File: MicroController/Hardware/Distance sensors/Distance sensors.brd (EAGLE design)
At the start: 87 x 55 mm, 39 parts, among them U1 LM2937IMP-5.0, U2 TXB0108PWR, U3 TLV1117-33CDCY, U4 TXB0108PWR, X1 0446200002, X2 0446200002, X3 0446200002

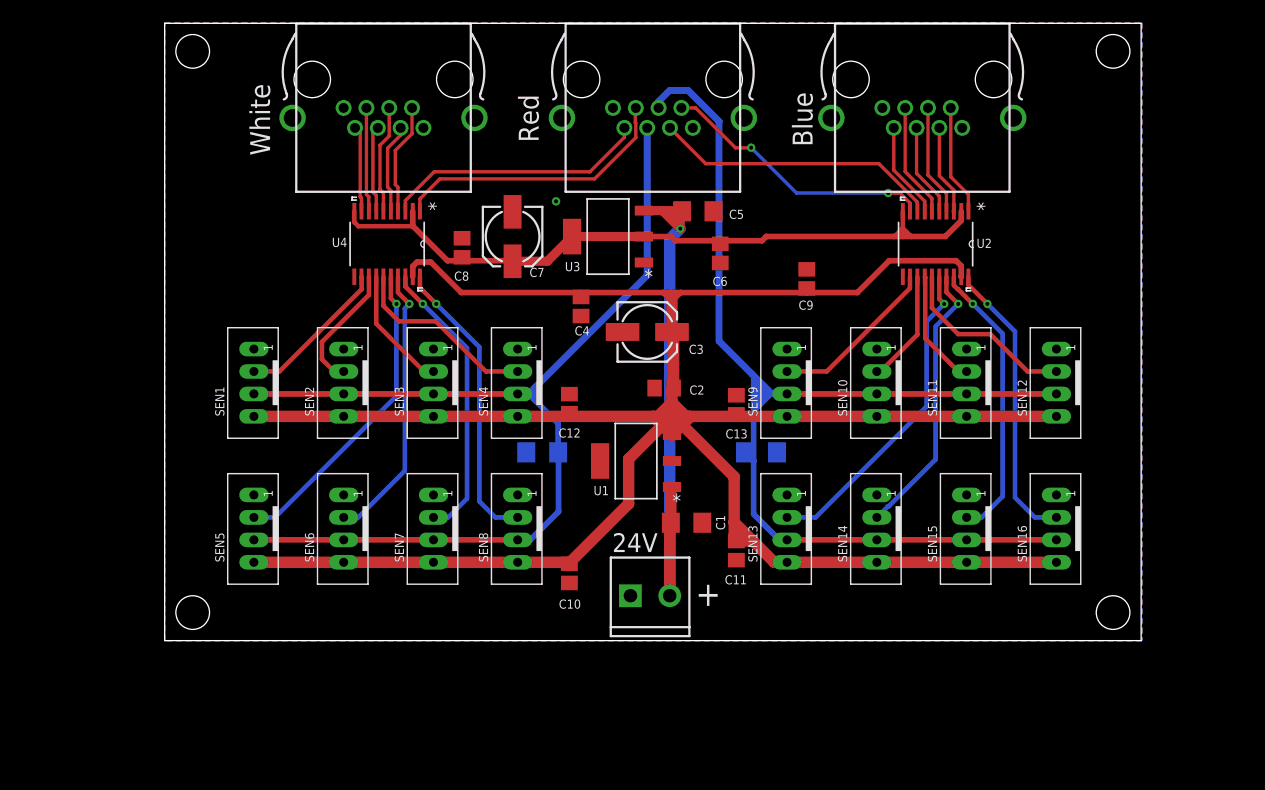
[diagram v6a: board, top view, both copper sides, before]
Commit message: The distance sensor PCB is close to finished.
There needs to be a final check before ordering the PCB. The PCB is not very complicated compared to the previous version, making it easier to check.
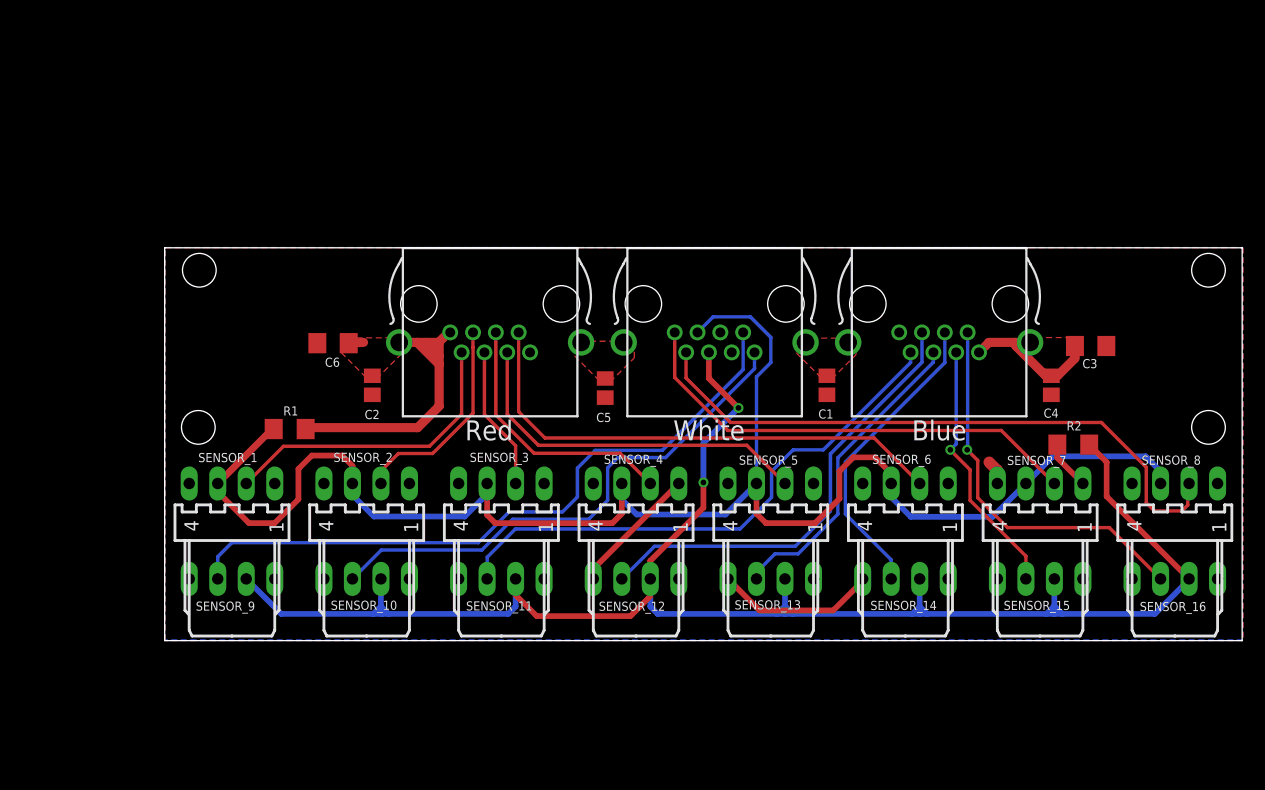
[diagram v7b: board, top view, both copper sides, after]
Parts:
- removed 24V: (no value), SparkFun-Connectors:SCREWTERMINAL-3.5MM-2
- removed C10, C11, C12, C13, C8, C9: (no value), adafruit:C0805
- removed C7: (no value), adafruit:153CLV-0505
- removed SEN1, SEN10, SEN11, SEN12, SEN13, SEN14, SEN15, SEN16, SEN2, SEN3, SEN4, SEN5, SEN6, SEN7, SEN8, SEN9: JST-PH_4-PIN_HEADER, SRG:JST_B4B-PH_HEADER
- removed U1: LM2937IMP-5.0, NSC_By_element14_Batch_1.1:SOT230P700X180-4N
- removed U2, U4: TXB0108PWR, Texas Instruments_By_element14_Batch_1:SOP65P640X120-20N
- removed U3: TLV1117-33CDCY, Texas Instruments_By_element14_Batch_1:SOT230P700X180-4N
- added SENSOR_1, SENSOR_10, SENSOR_11, SENSOR_12, SENSOR_13, SENSOR_14, SENSOR_15, SENSOR_16, SENSOR_2, SENSOR_3, SENSOR_4, SENSOR_5, SENSOR_6, SENSOR_7, SENSOR_8, SENSOR_9: 22-05-7048-04, con-molex:7395-04
- C1, C5: device adafruit:C1206 -> adafruit:C0805
- C3: device adafruit:153CLV-0505 -> adafruit:C1206
- C6: device adafruit:C0805 -> adafruit:C1206
- moved C4 42.5 mm to (79.0, 22.8), turned to 90 degrees
- moved C3 39.5 mm to (82.5, 26.2), turned to 180 degrees
- moved C6 35.4 mm to (15.0, 26.5), turned to 0 degrees
- moved R2 27.8 mm to (81.0, 17.5), flipped to the top
- moved C2 26.0 mm to (18.5, 22.8), turned to 90 degrees
- moved R1 22.6 mm to (11.1, 18.9), flipped to the top
- moved X1 22.1 mm to (29.0, 30.0)
- moved X2 20.7 mm to (49.0, 30.0)
- moved X3 20.1 mm to (69.0, 30.0)
- moved C5 17.8 mm to (39.2, 22.5), turned to 90 degrees
- moved C1 17.5 mm to (59.0, 22.8), turned to 90 degrees
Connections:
- removed net +24V: 24V.2, C1.1, C5.1, U1.1, U3.3
- removed net +3V3: C6.1, C7.+, C8.1, U2.10, U2.2, U3.2, U3.4, U4.10, U4.2
- removed net ULTRAS1: SEN1.P2, U4.12
- removed net ULTRAS10: SEN10.P2, U2.13
- removed net ULTRAS11: SEN11.P2, U2.14
- removed net ULTRAS12: SEN12.P2, U2.15
- removed net ULTRAS13: SEN13.P2, U2.16
- removed net ULTRAS14: SEN14.P2, U2.17
- removed net ULTRAS15: SEN15.P2, U2.18
- removed net ULTRAS16: SEN16.P2, U2.20
- removed net ULTRAS2: SEN2.P2, U4.13
- removed net ULTRAS3: SEN3.P2, U4.14
- removed net ULTRAS4: SEN4.P2, U4.15
- removed net ULTRAS5: SEN5.P2, U4.16
- removed net ULTRAS6: SEN6.P2, U4.17
- removed net ULTRAS7: SEN7.P2, U4.18
- removed net ULTRAS8: SEN8.P2, U4.20
- removed net ULTRAS9: SEN9.P2, U2.12
- net +5V: now also C1.1, C3.1, C5.1, C6.1, SENSOR_1.4, SENSOR_10.4, SENSOR_11.4, SENSOR_12.4, SENSOR_13.4, SENSOR_14.4, SENSOR_15.4, SENSOR_16.4, SENSOR_2.4, SENSOR_3.4, SENSOR_4.4, SENSOR_5.4, SENSOR_6.4, SENSOR_7.4, SENSOR_8.4, SENSOR_9.4, X2.5, X2.6; no longer C10.1, C11.1, C12.1, C13.1, C3.+, C9.1, SEN1.P4, SEN10.P4, SEN11.P4, SEN12.P4, SEN13.P4, SEN14.P4, SEN15.P4, SEN16.P4, SEN2.P4, SEN3.P4, SEN4.P4, SEN5.P4, SEN6.P4, SEN7.P4, SEN8.P4, SEN9.P4, U1.3, U2.19, U4.19
- net GND: now also C3.2, SENSOR_1.1, SENSOR_10.1, SENSOR_11.1, SENSOR_12.1, SENSOR_13.1, SENSOR_14.1, SENSOR_15.1, SENSOR_16.1, SENSOR_2.1, SENSOR_3.1, SENSOR_4.1, SENSOR_5.1, SENSOR_6.1, SENSOR_7.1, SENSOR_8.1, SENSOR_9.1; no longer 24V.1, C10.2, C11.2, C12.2, C13.2, C3.-, C7.-, C8.2, C9.2, SEN1.P1, SEN10.P1, SEN11.P1, SEN12.P1, SEN13.P1, SEN14.P1, SEN15.P1, SEN16.P1, SEN2.P1, SEN3.P1, SEN4.P1, SEN5.P1, SEN6.P1, SEN7.P1, SEN8.P1, SEN9.P1, U1.2, U1.4, U2.11, U3.1, U4.11, X2.1, X2.8
- net TRIGGER_1: now also SENSOR_1.3, SENSOR_2.3, SENSOR_3.3, SENSOR_4.3, SENSOR_5.3, SENSOR_6.3, SENSOR_7.3, SENSOR_8.3, X2.3; no longer SEN1.P3, SEN2.P3, SEN3.P3, SEN4.P3, SEN5.P3, SEN6.P3, SEN7.P3, SEN8.P3, X2.4
- net TRIGGER_2: now also SENSOR_10.3, SENSOR_11.3, SENSOR_12.3, SENSOR_13.3, SENSOR_14.3, SENSOR_15.3, SENSOR_16.3, SENSOR_9.3, X2.4; no longer SEN10.P3, SEN11.P3, SEN12.P3, SEN13.P3, SEN14.P3, SEN15.P3, SEN16.P3, SEN9.P3, X2.5
- net ULTRA1: now also SENSOR_1.2; no longer U4.9
- net ULTRA10: now also SENSOR_10.2, X2.8; no longer U2.8, X2.6
- net ULTRA11: now also SENSOR_11.2; no longer U2.7
- net ULTRA12: now also SENSOR_12.2; no longer U2.6
- net ULTRA13: now also SENSOR_13.2; no longer U2.5
- net ULTRA14: now also SENSOR_14.2; no longer U2.4
- net ULTRA15: now also SENSOR_15.2; no longer U2.3
- net ULTRA16: now also SENSOR_16.2; no longer U2.1
- net ULTRA2: now also SENSOR_2.2; no longer U4.8
- net ULTRA3: now also SENSOR_3.2; no longer U4.7
- net ULTRA4: now also SENSOR_4.2; no longer U4.6
- net ULTRA5: now also SENSOR_5.2; no longer U4.5
- net ULTRA6: now also SENSOR_6.2; no longer U4.4
- net ULTRA7: now also SENSOR_7.2, X2.1; no longer U4.3, X2.2
- net ULTRA8: now also SENSOR_8.2, X2.2; no longer U4.1, X2.3
- net ULTRA9: now also SENSOR_9.2; no longer U2.9
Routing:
- net +5V: track 238.0 -> 2.26 mm
- net GND: track 0.00 -> 73.0 mm, vias 1 -> 0
- net +3V3: track 65.6 -> 0.00 mm
- net TRIGGER_1: track 93.4 -> 147.8 mm
- net TRIGGER_2: track 106.9 -> 157.1 mm, vias 0 -> 2
- net +24V: track 50.2 -> 0.00 mm, vias 1 -> 0
- net ULTRA11: track 8.58 -> 49.1 mm
- net ULTRA9: track 24.6 -> 60.5 mm, vias 2 -> 0
- net ULTRA6: track 9.92 -> 45.4 mm
- net ULTRA8: track 25.3 -> 55.9 mm
- net ULTRA12: track 10.2 -> 40.4 mm
- net ULTRAS13: track 28.9 -> 0.00 mm, vias 1 -> 0
- net ULTRAS5: track 28.0 -> 0.00 mm, vias 1 -> 0
- net ULTRAS8: track 26.2 -> 0.00 mm, vias 1 -> 0
- net ULTRAS16: track 25.8 -> 0.00 mm, vias 1 -> 0
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- added copper zone on layer 1, net +5V
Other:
- board size 87 x 55 mm -> 96 x 35 mm
- board text removed: "+"
